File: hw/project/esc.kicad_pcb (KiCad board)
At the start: 4 copper layers, 125 x 80 mm, 185 parts, among them J1 KFA-1016-10_16-2P, J10 I2C, J11 Misc, J12 Voltage Monitor, J2 KFA-1016-10_16-3P, J3 FTSH-107-01-L-DV-K-A, J4 Throttle, J5 Hall, J6 Serial, J7 2.54 Comm, J8 SPI, J9 CAN, Q1 SUM110P06-08L-E3, Q2 SUM110P06-08L-E3, Q3 STL110N10F7, Q4 STL110N10F7, Q5 STL110N10F7, Q6 STL110N10F7, Q7 STL110N10F7, Q8 STL110N10F7, SW1 BOOT0, SW2 RESET, SW3 USER, U1 STSPIN32G4, U2 LMR51610XDBVR, U3 ATA6561-GAQW-N, X1 SWXC5ACVF0-32.000000

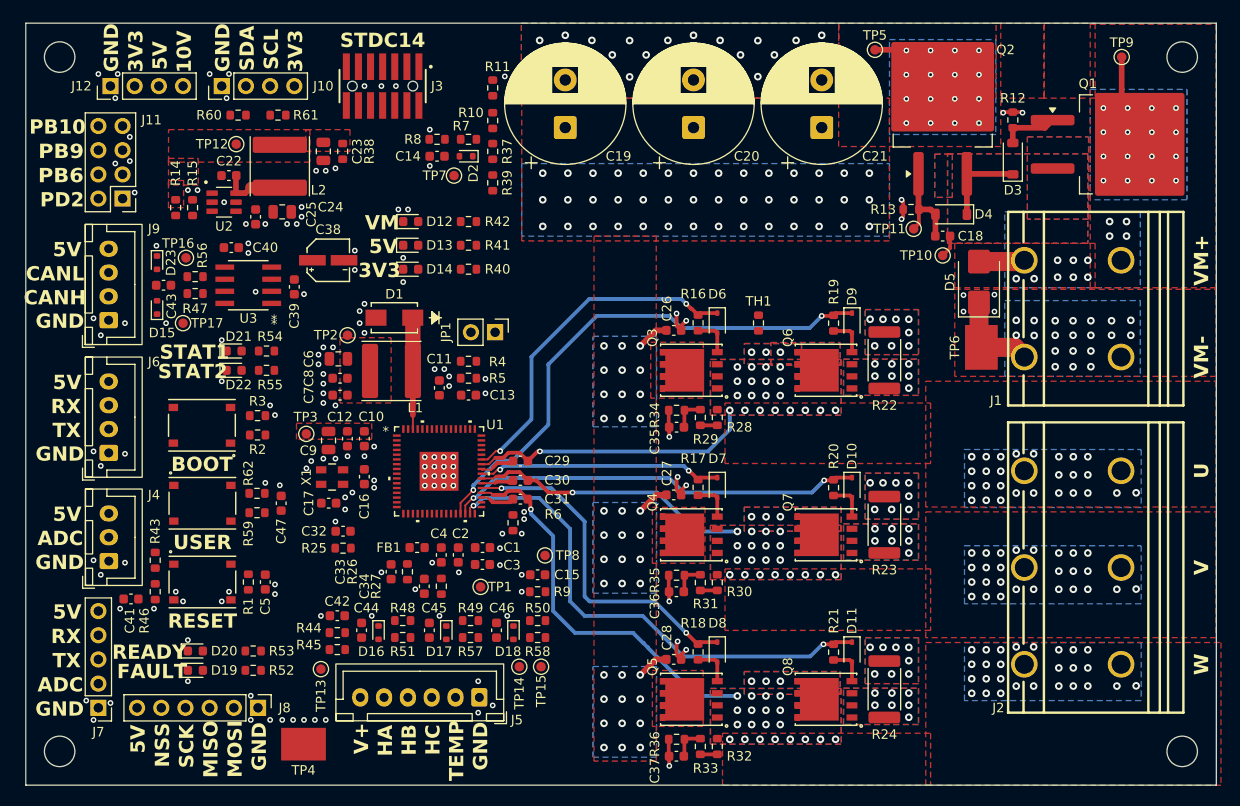
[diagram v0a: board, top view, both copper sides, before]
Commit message: Trace everything on power section except voltage sense resistors
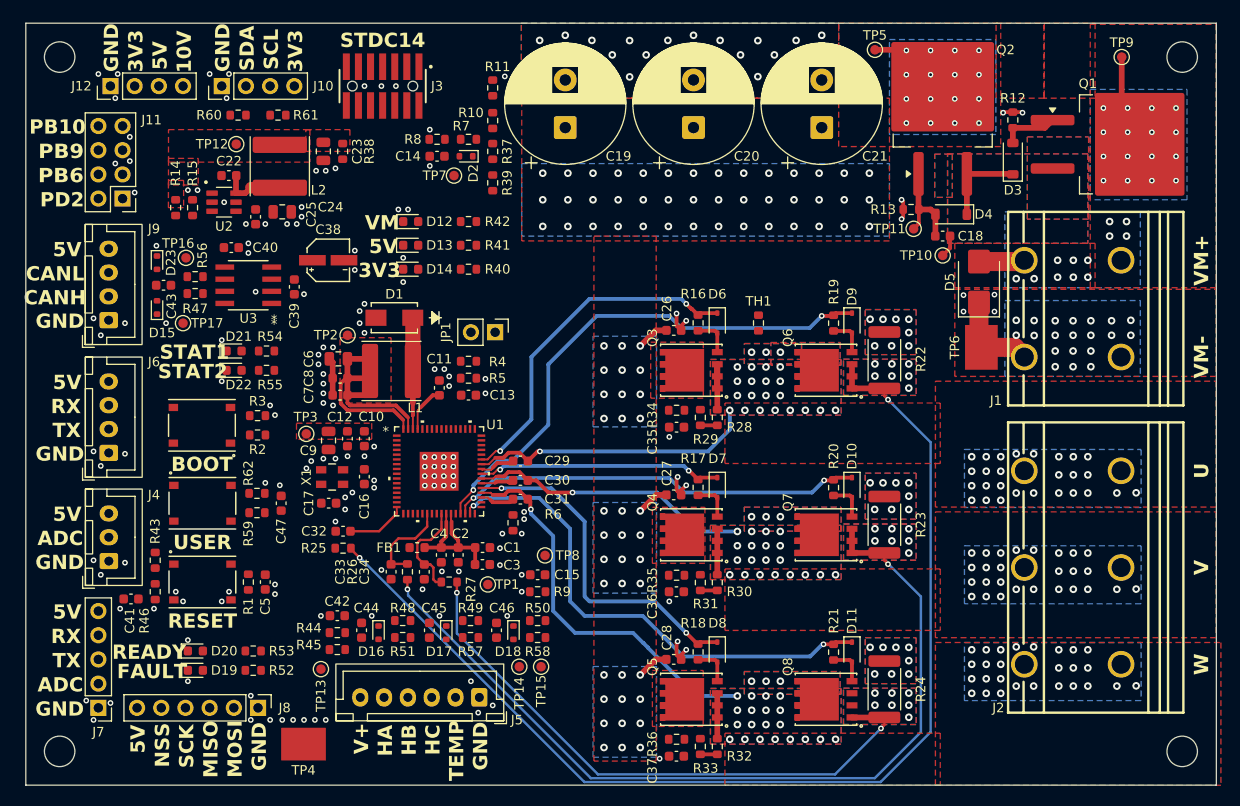
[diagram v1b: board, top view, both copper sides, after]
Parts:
- moved C34 1.51 mm to (53.8, 69.5)
- moved R27 0.94 mm to (56.4, 70.6), turned to 180 degrees
- moved TP1 0.80 mm to (60.5, 70.9)
- turned R25 to 180 degrees
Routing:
- net /Drive/VSHUNT_U+: track 0.00 -> 117.3 mm, vias 7 -> 9
- net /Drive/VSHUNT_V+: track 0.00 -> 91.8 mm, vias 7 -> 9
- net /Drive/VSHUNT_W+: track 0.00 -> 62.7 mm, vias 7 -> 9
- net VCC: track 0.00 -> 34.8 mm
- net VDDA: track 0.00 -> 14.7 mm
- net /Control/OPN_W: track 0.00 -> 10.6 mm
- net /Control/OPN_V: track 0.00 -> 9.67 mm
- net GND: track 8.41 -> 0.23 mm
- net /Drive/U: track 30.5 -> 37.8 mm
- net /Control/OPN_U: track 0.00 -> 6.31 mm
- net VM: track 19.2 -> 24.1 mm
- net /Drive/V: track 29.7 -> 34.6 mm
- net /Drive/W: track 41.4 -> 46.2 mm
- net PGND: track 23.9 -> 27.9 mm
- net /Control/VPHASE_U: track 3.50 -> 0.17 mm
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
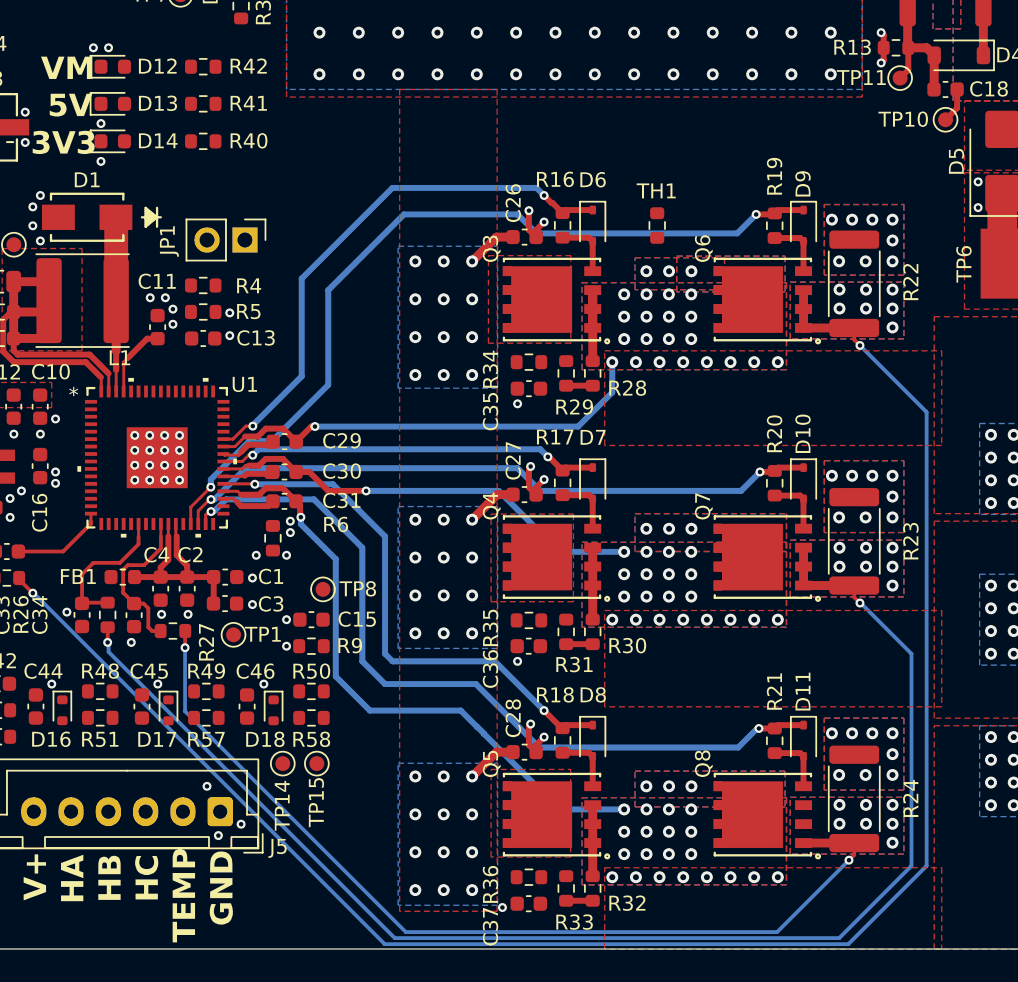
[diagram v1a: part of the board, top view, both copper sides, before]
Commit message: Route everything on the high-power side
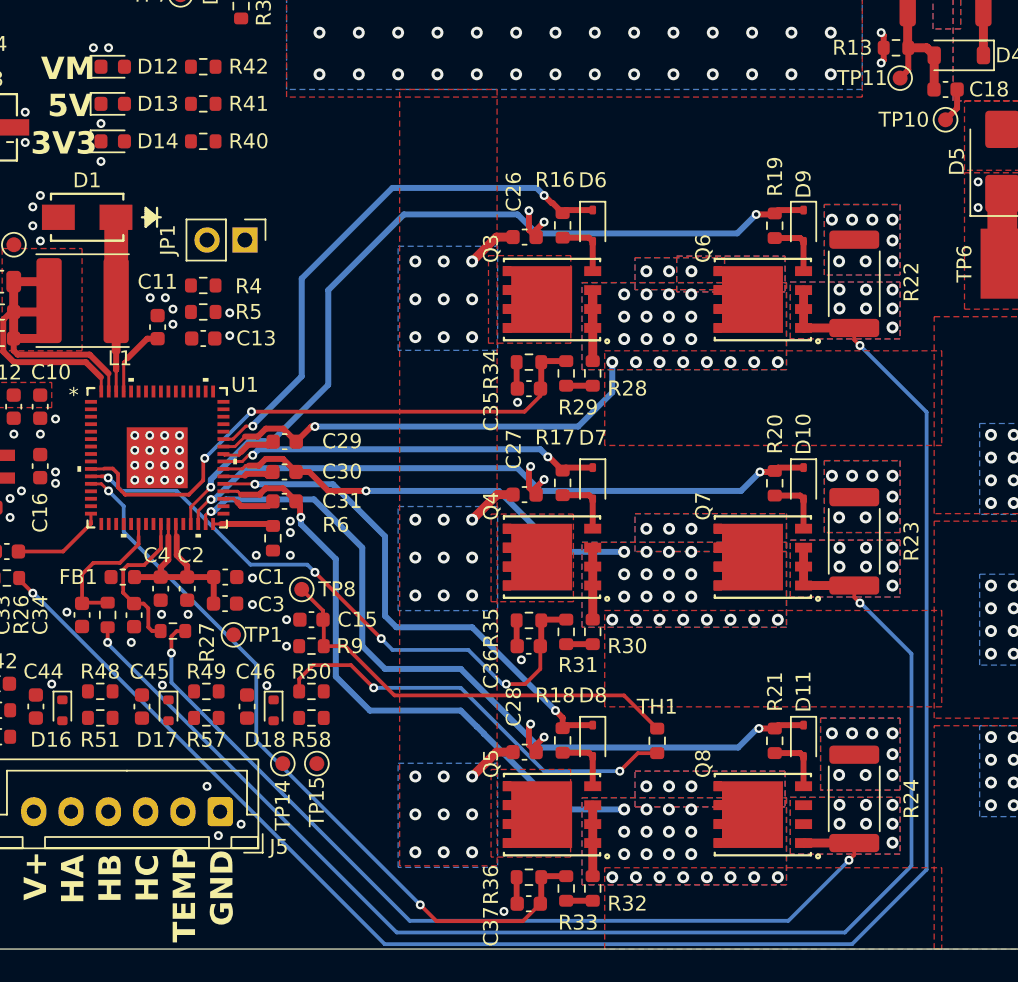
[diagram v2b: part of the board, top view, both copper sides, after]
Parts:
- moved TH1 34.6 mm to (88.9, 78.0), turned to 90 degrees
- moved TP8 1.43 mm to (65.0, 67.8)
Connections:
- TH1 pad 1: VDDA -> VDD
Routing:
- net /Control/VPHASE_W: track 0.19 -> 50.3 mm, vias 0 -> 2
- net /Control/VPHASE_V: track 0.17 -> 41.7 mm, vias 0 -> 4
- net /Control/VPHASE_U: track 0.17 -> 39.0 mm, vias 0 -> 2
- net /Control/PCB_TEMP: track 0.00 -> 29.1 mm
- net VDD: track 0.00 -> 28.7 mm, vias 0 -> 2
- net GND: track 0.23 -> 5.43 mm
- net PGND: track 27.9 -> 32.0 mm
- net /Control/GHS3: track 36.2 -> 35.2 mm
- net /Control/GLS3: track 53.1 -> 52.5 mm
- net VM: vias 94 -> 85

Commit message: Route all power sections
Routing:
- net GND: track 5.43 -> 46.7 mm
- net PGND: track 32.0 -> 57.6 mm
- net VDD: track 28.7 -> 47.9 mm
- net /Control/OSC_OUT: track 0.00 -> 12.6 mm
- net /Control/SCREF: track 0.00 -> 7.07 mm
- net 5V: track 0.00 -> 6.78 mm
- net /Control/OSC_IN: track 0.00 -> 6.09 mm
- net VM: track 24.1 -> 29.1 mm
- net Net-(U2-FB): track 0.00 -> 4.01 mm
- net Net-(U2-CB): track 0.00 -> 2.34 mm

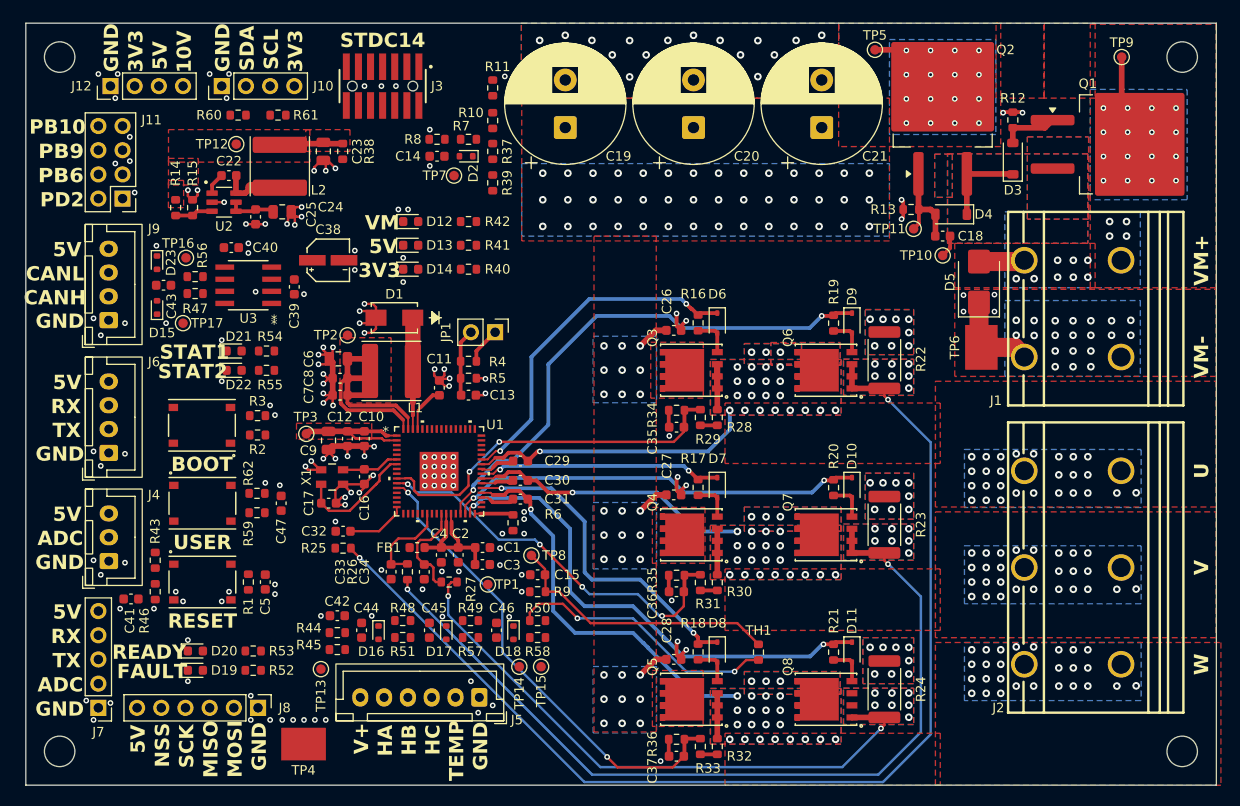
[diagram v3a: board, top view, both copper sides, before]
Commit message: Route all major interfaces
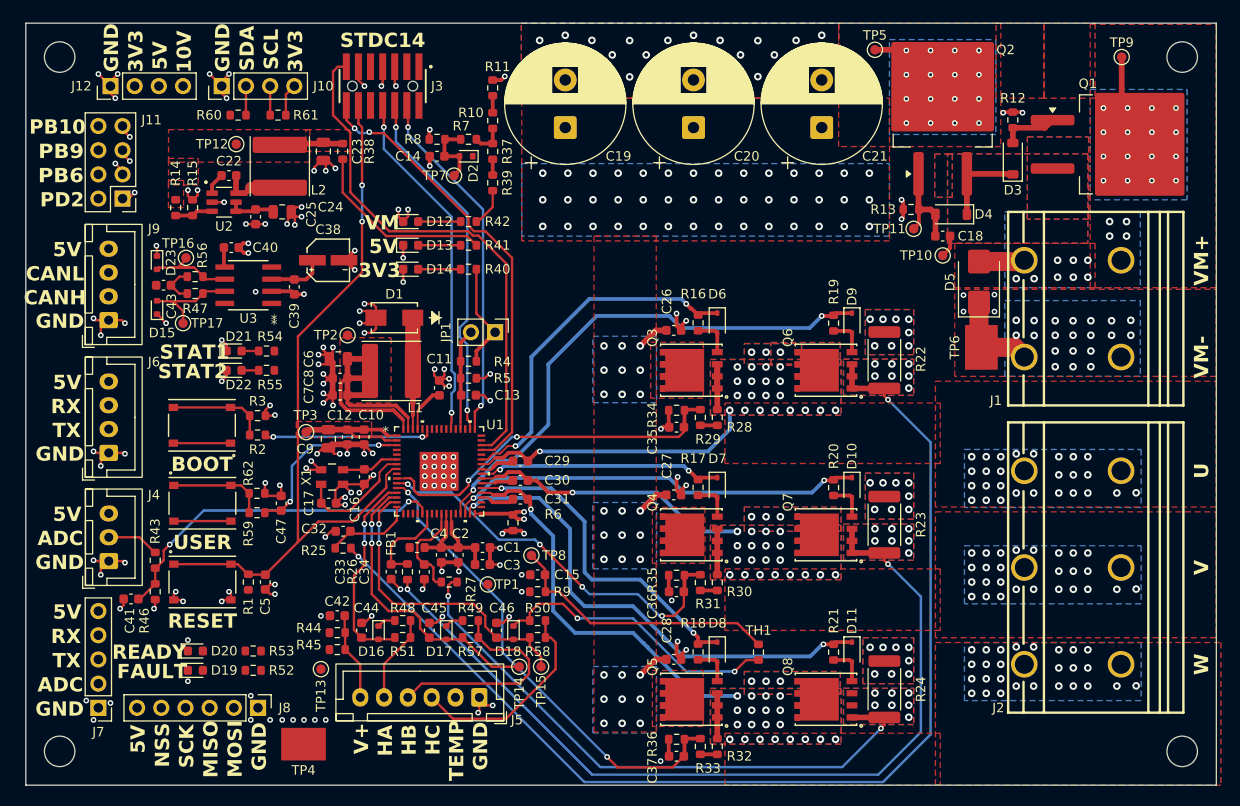
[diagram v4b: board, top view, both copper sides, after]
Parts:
- moved C10 0.18 mm to (47.5, 55.4)
- moved C12 0.18 mm to (45.7, 55.4)
- moved TP3 0.18 mm to (41.4, 54.9)
- moved C9 0.18 mm to (43.7, 55.6)
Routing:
- net GND: track 46.7 -> 143.5 mm, vias 124 -> 123
- net /Control/NRST: track 0.00 -> 78.0 mm, vias 0 -> 2
- net /Control/RX: track 0.00 -> 55.3 mm
- net /Control/TX: track 0.00 -> 47.9 mm, vias 0 -> 2
- net /Control/SWCLK: track 0.00 -> 37.9 mm, vias 0 -> 2
- net /Control/SWDIO: track 0.00 -> 37.6 mm, vias 0 -> 2
- net /Control/TRACESWO: track 0.00 -> 37.3 mm, vias 0 -> 2
- net /Control/ADC: track 0.00 -> 36.5 mm, vias 0 -> 2
- net /Control/HC: track 0.00 -> 32.6 mm, vias 0 -> 2
- net /Control/HB: track 0.00 -> 31.1 mm, vias 0 -> 2
- net VDD: track 47.9 -> 78.9 mm
- net Net-(J5-Pin_4): track 0.00 -> 23.3 mm
- net Net-(J5-Pin_3): track 0.00 -> 21.9 mm
- net /Control/HA: track 0.00 -> 21.6 mm, vias 0 -> 2
- net Net-(R38-Pad2): track 0.00 -> 19.8 mm
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
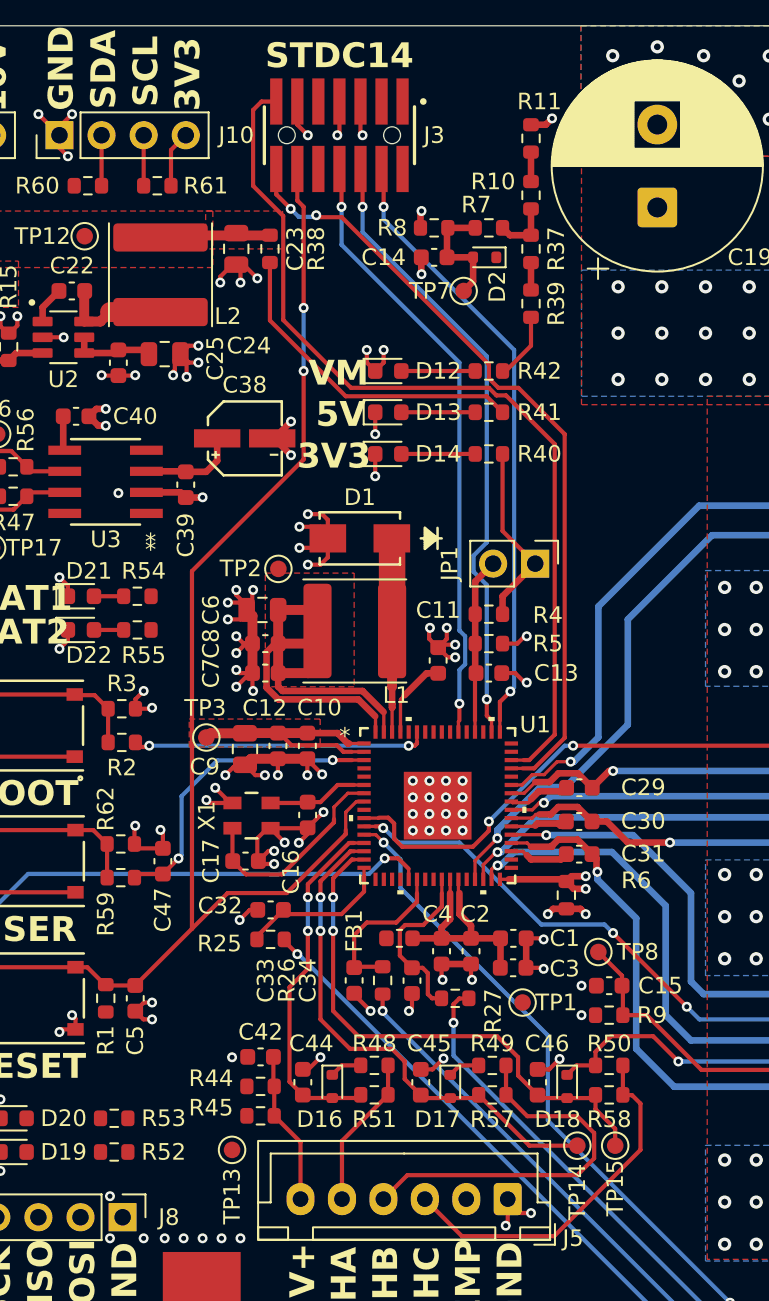
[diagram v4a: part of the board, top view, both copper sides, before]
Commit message: Traces left are VM_SENSE, LEDs, CAN, and headers
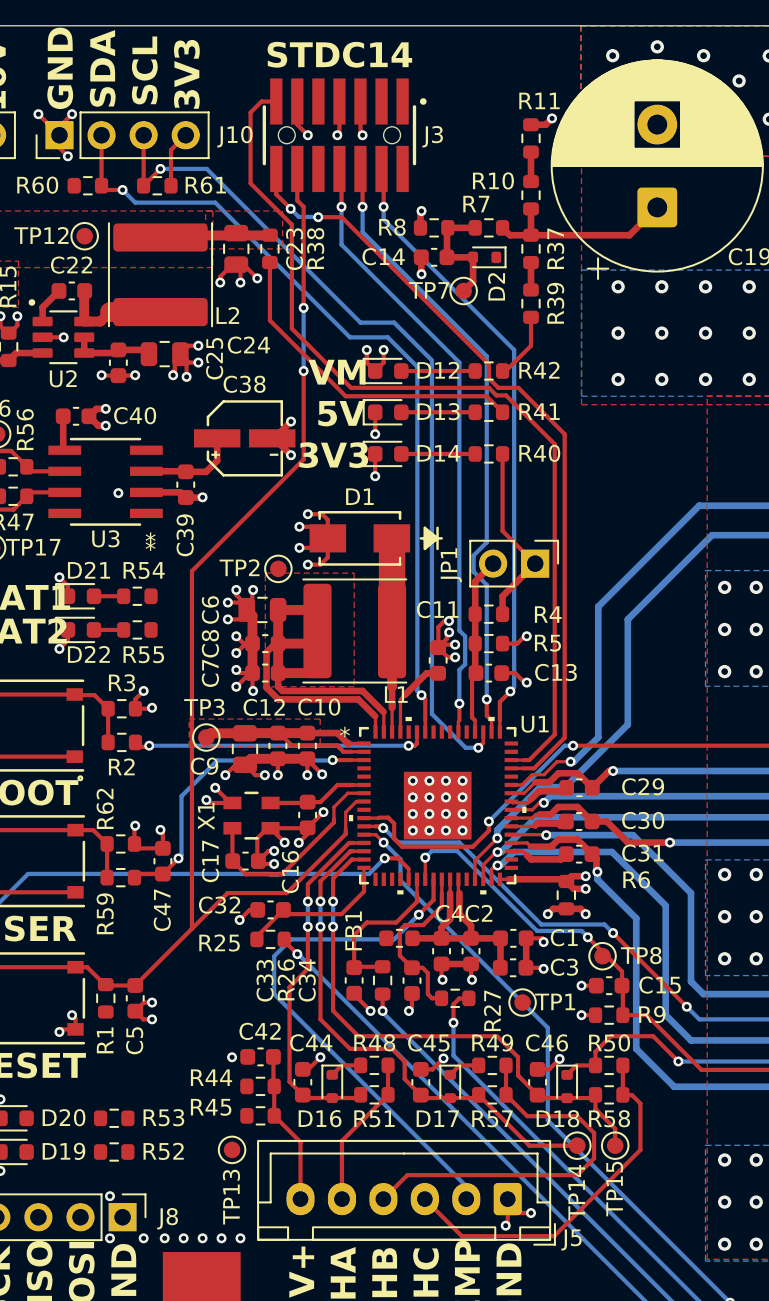
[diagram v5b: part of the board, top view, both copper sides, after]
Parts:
- moved TP8 0.36 mm to (65.3, 68.1)
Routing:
- net /Control/SCL: track 3.05 -> 51.7 mm, vias 0 -> 2
- net /Control/SDA: track 3.05 -> 48.9 mm, vias 0 -> 2
- net /Control/MOTOR_TEMP: track 0.00 -> 31.7 mm, vias 0 -> 1
- net /Control/PCB_TEMP: track 29.1 -> 43.7 mm, vias 0 -> 2
- net VM: track 32.6 -> 40.9 mm
- net GND: track 143.5 -> 145.4 mm
